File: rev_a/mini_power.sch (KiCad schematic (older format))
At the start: 4 parts

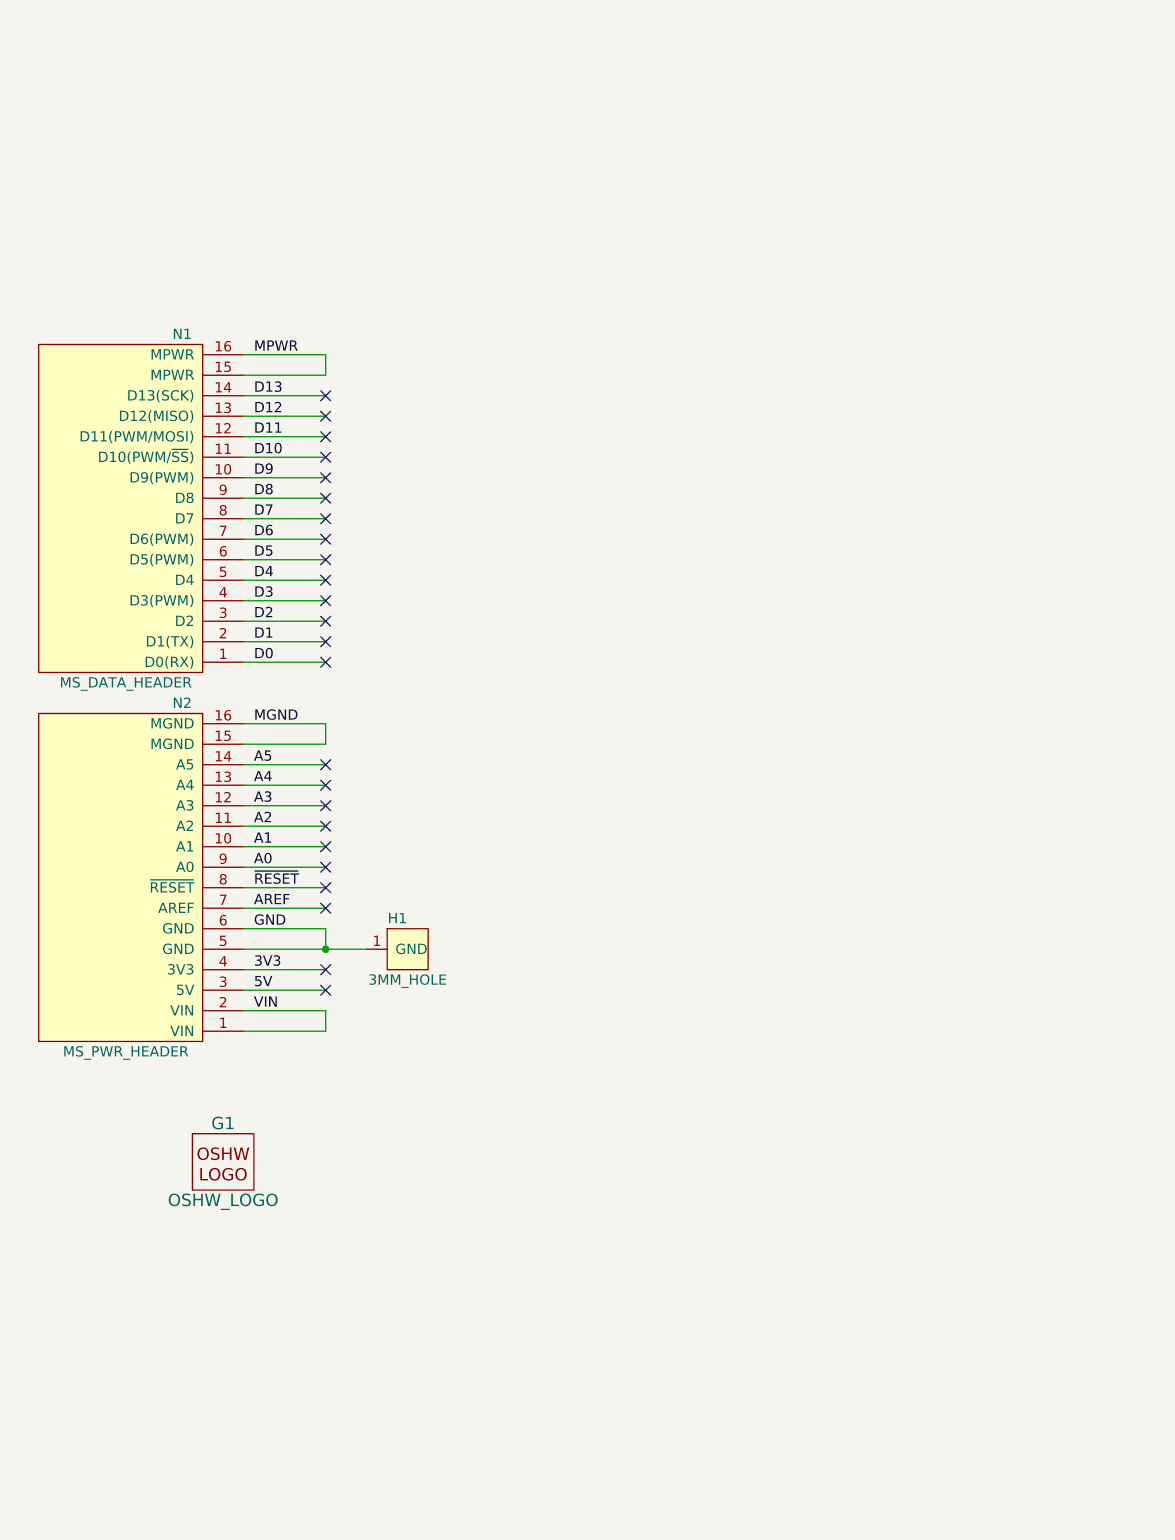
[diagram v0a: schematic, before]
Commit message: Did initial schematic for power mini-shield.
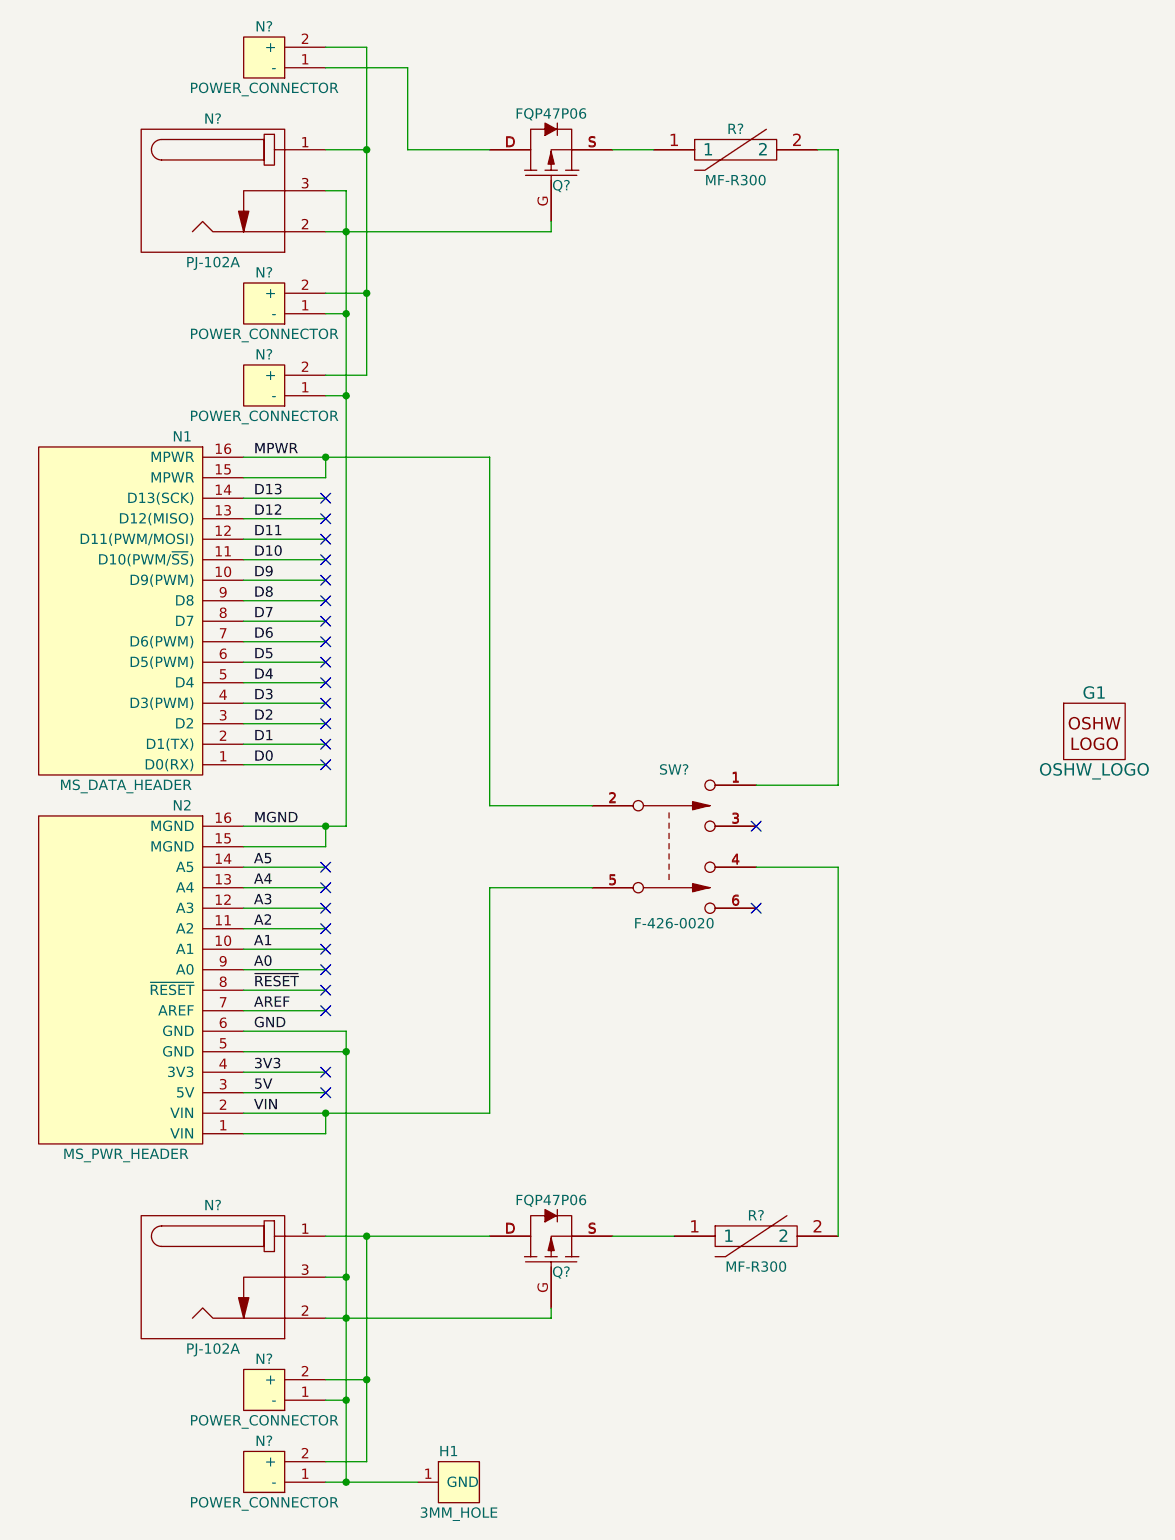
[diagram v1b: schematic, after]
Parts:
- added N? (x2): PJ-102A, symbol BARREL_POWER_CONNECTOR
- added N? (x5): POWER_CONNECTOR, symbol POWER_CONNECTOR
- added Q? (x2): FQP47P06, symbol P_CHANNEL_MOSET_HORIZ
- added R? (x2): MF-R300, symbol RESETABLE_FUSE
- added SW?: F-426-0020, symbol DPDT
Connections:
- net MGND is gone; now on net -: N2.15 (MGND), N2.16 (MGND)
- net MPWR: now also SW?.2
- net VIN: now also SW?.5
- net GND renamed -
- net -: now also N?.1 (-), N?.1 (-), N?.1 (-), N?.1 (-), N?.2 (-), N?.2 (-), N?.3 (-), N?.3 (-), Q?.G, Q?.G
- new net: N?.1 (+), N?.2 (+), N?.2 (+), N?.2 (+)
- new net: N?.1 (-), Q?.D
- new net: Q?.S, R?.1 (x2)
- new net: R?.2, SW?.1
- new net: R?.2, SW?.4
- new net: N?.1 (+), N?.2 (+), N?.2 (+), Q?.D
- no-connect marks 24 -> 26
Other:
- moved on the sheet: G1, H1, N1, N2

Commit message: Did initial board layout.
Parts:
- removed N1: MS_DATA_HEADER, symbol MS_DATA_HEADER
- removed N2: MS_PWR_HEADER, symbol MS_PWR_HEADER
- removed N? (x2): PJ-102A, symbol BARREL_POWER_CONNECTOR
- removed N?: POWER_CONNECTOR, symbol POWER_CONNECTOR
- removed R?: MF-R300, symbol RESETABLE_FUSE
- added N1: MS_DATA_HEADER_POWER, symbol MS_DATA_HEADER_POWER
- added N2: MS_PWR_HEADER_POWER, symbol MS_PWR_HEADER_POWER
- added N3: OSTTC020162, symbol POWER_CONNECTOR_ALT
- added R2: RESETABLE_FUSE, symbol RESETABLE_FUSE
- N4, N5, N6, N7: renamed from N?; value POWER_CONNECTOR -> OSTTC020162
- gave numbers to parts that had none: 4
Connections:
- net 3V3: now also N2.4 (3V3)
- net 5V: now also N2.3 (5V)
- net A0: now also N2.9 (A0)
- net A1: now also N2.10 (A1)
- net A2: now also N2.11 (A2)
- net A3: now also N2.12 (A3)
- net A4: now also N2.13 (A4)
- net A5: now also N2.14 (A5)
- net AREF: now also N2.7 (AREF)
- net D0: now also N1.1 (D0(RX))
- net D1: now also N1.2 (D1(TX))
- net D10: now also N1.11 (D10(PWM/~SS))
- net D11: now also N1.12 (D11(PWM/MOSI))
- net D12: now also N1.13 (D12(MISO))
- net D13: now also N1.14 (D13(SCK))
- net D2: now also N1.3 (D2)
- net D3: now also N1.4 (D3(PWM))
- net D4: now also N1.5 (D4)
- net D5: now also N1.6 (D5(PWM))
- net D6: now also N1.7 (D6(PWM))
- net D7: now also N1.8 (D7)
- net D8: now also N1.9 (D8)
- net D9: now also N1.10 (D9(PWM))
- net MPWR: now also N1.15 (MPWR), N1.16 (MPWR)
- net VIN: now also N2.1 (VIN), N2.2 (VIN)
- net ~RESET: now also N2.8 (~RESET)
- net LPWR4: now reaches N4.2 (+), N5.2 (+)
- net LPWR4: now also N3.2 (+)
- net MPWR1: now reaches Q1.D
- net MPWR1: now also N3.1 (-)
- net MPWR2: now reaches Q1.S, R1.1
- net MPWR3: now reaches R1.2, SW1.1
- net LPWR3: now reaches SW1.4
- net LPWR3: now also R2.2
- net LPWR1: now reaches N6.2 (+), N7.2 (+), Q2.D
- net LPWR2: now reaches Q2.S
- net LPWR2: now also R2.1
- net - renamed GND
- net GND: now also N2.5 (GND), N2.6 (GND); no longer N4.1 (-), N5.1 (-), Q1.G
- new net MGND: N2.15 (MGND), N2.16 (MGND), N4.1 (-), N5.1 (-), Q1.G
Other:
- note added: "Daisy Chain\nMotor Power"
- note added: "Logic Power\nDaisy Chain"
- note added: "Motor\nEmergency Stop"
- moved on the sheet: H1, N6, N7, Q1, R1
